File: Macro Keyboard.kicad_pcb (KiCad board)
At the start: 2 copper layers, 101.6 x 123.4 mm, 132 parts, among them J2901 FPC 1x24, Q2901 Q_PJFET_GDS, SW1001 KH-PS1611-54, SW1101 KH-PS1611-54, SW1201 KH-PS1611-54, SW1301 KH-PS1611-54, SW1401 KH-PS1611-54, SW1501 KH-PS1611-54, SW2801 SWITCH TACTILE SPST-NO 50MA 1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, SW601 KH-PS1611-54, SW701 KH-PS1611-54, SW801 KH-PS1611-54, SW901 KH-PS1611-54, U2701 PCA9745BTWJ, U2801 Pico-JER, U301 VEML7700, U401 PI4ULS5V201TAEX

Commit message: Moved everything to the back that I wanted. Added fun things :)
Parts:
- removed the Ref** at (116.8, 32.8)
- added Ref**: Val**, Macro Keyboard:TMPCB Logo bottom silk 10mm, F.Cu at (133.3, 42.8)
- added svg2mod: G***, Macro Keyboard:kilroy, F.Cu at (82.8, 137.0)
- added svg2mod: G***, Macro Keyboard:xkcd-swing, F.Cu at (97.8, 111.0)
- added svg2mod: G***, Macro Keyboard:xkcd-climb, F.Cu at (106.4, 44.4)
- added svg2mod: G***, Macro Keyboard:xkcd, F.Cu at (110.2, 72.9)
- C2701, C2801, C2901, C2902, C2903, C2907, C2908, C2909, C301, C401, C402, D2901, D2902, D2903, L2901, Q2901, R208, R209, R2704, R2705, R2706, R2707, R2801, R2902, R301, R302, U2701, U401: moved to B.Cu
- moved D2901 23.7 mm to (95.5, 50.8), turned to 22.5 degrees
- moved DS** 23.6 mm to (73.0, 59.5)
- moved D2903 23.1 mm to (94.9, 47.6)
- moved R2801 20.1 mm to (103.2, 26.3), turned to 45 degrees
- moved C2906 15.0 mm to (117.1, 74.3), turned to 90 degrees
- moved C2907 14.2 mm to (115.1, 74.3), turned to 270 degrees
- moved R2703 12.6 mm to (131.7, 69.1), turned to 0 degrees
- moved U301 12.5 mm to (92.8, 38.6), turned to 90 degrees
- moved C2701 11.8 mm to (130.8, 64.5)
- moved C2903 11.5 mm to (113.0, 74.3), turned to 270 degrees
- moved R2704 11.2 mm to (131.7, 71.1), turned to 0 degrees
- moved C2905 9.65 mm to (100.1, 52.0), turned to 0 degrees
- moved R302 7.30 mm to (97.7, 36.4), turned to 90 degrees
- moved R2706 7.22 mm to (128.4, 60.0)
- moved C401 7.05 mm to (136.9, 51.2), turned to 0 degrees
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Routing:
- net GND: track 117.9 -> 188.2 mm, vias 114 -> 120
- net /eInk Display/DS_VGH: track 7.88 -> 41.7 mm, vias 0 -> 2
- net Net-(C2902-Pad2): track 44.5 -> 12.8 mm, vias 2 -> 0
- net /eInk Display/DS_VGL: track 10.5 -> 41.9 mm, vias 0 -> 2
- net +5V: track 336.2 -> 359.3 mm, vias 7 -> 3
- net /eInk Display/DS_VDDD: track 5.58 -> 21.9 mm
- net /eInk Display/DS_MOSFET_S: track 31.9 -> 16.2 mm, vias 4 -> 0
- net /RGB Driver/DRIVER_LED_CS_3V3: track 48.4 -> 63.5 mm, vias 2 -> 0
- net /Pico/GPIO_14: track 64.7 -> 49.9 mm, vias 4 -> 2
- net /RGB Driver/DRIVER_LED_SW2_G_5V: track 54.5 -> 40.3 mm, vias 0 -> 1
- net /eInk Display/DS_VSH: track 6.16 -> 19.4 mm, vias 0 -> 1
- net /RGB Driver/DRIVER_LED_SW2_B_5V: track 53.6 -> 40.3 mm, vias 0 -> 1
- net /Pico/GPIO_20: track 60.7 -> 48.2 mm, vias 1 -> 2
- net /Level Converter/D_IN_3V3: track 87.6 -> 99.5 mm, vias 1 -> 2
- net SPI_MISO_3V: track 24.5 -> 36.3 mm, vias 1 -> 0
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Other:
- board text added: "0"
- board text added: "1"
- board text added: "2"
- board text added: "Designed in Washington State"
- board text added: "IF YOU CAN READ THIS, THERE IS A PROBLEM …OR MAYBE THE BOARD HAS NOT BEEN ASSEMBLED"
- board text added: "pew pew"
- board text added: "π"

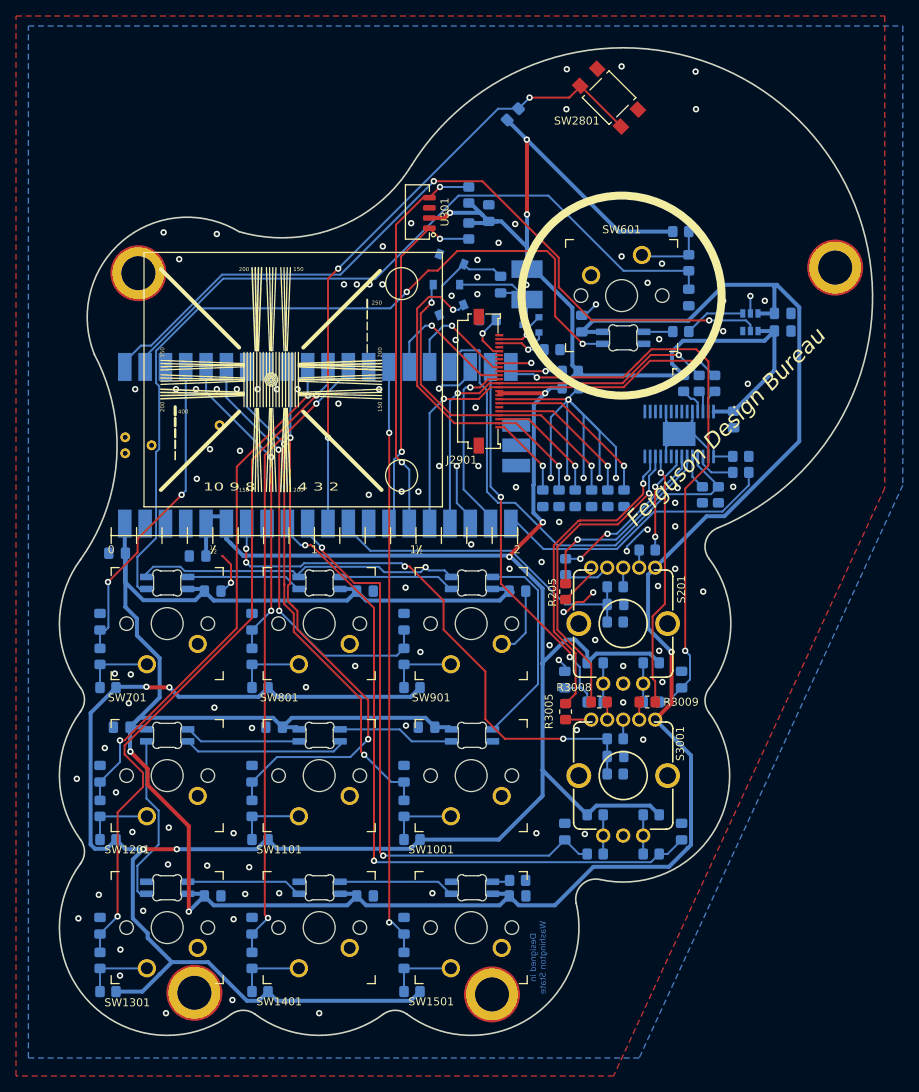
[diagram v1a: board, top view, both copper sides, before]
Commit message: Updated silkscreen outlines. Added epaper cad part.
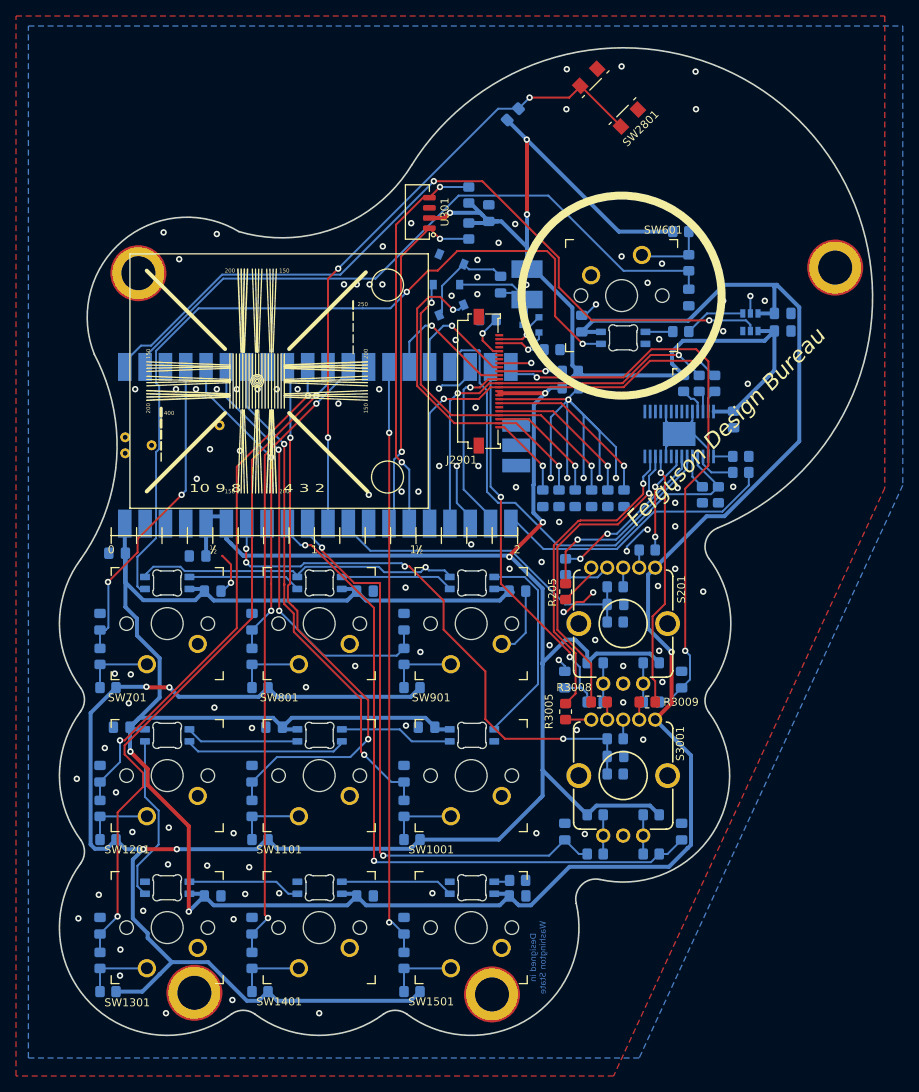
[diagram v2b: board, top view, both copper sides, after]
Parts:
- moved DS** 1.77 mm to (71.2, 59.7)
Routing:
- net +5V: track 359.3 -> 358.7 mm

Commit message: Add Solder Mask Clearance
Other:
- rule pad_to_mask_clearance: 0 -> 0.00129
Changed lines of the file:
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@@
   (layers
     (0 F.Cu signal)
-    (31 B.Cu signal hide)
+    (31 B.Cu signal)
     (32 B.Adhes user hide)
     (33 F.Adhes user hide)
@@
     (mod_text_size 1 1)
     (mod_text_width 0.15)
-    (pad_size 1.524 1.524)
-    (pad_drill 0.762)
-    (pad_to_mask_clearance 0)
+    (pad_size 1.7018 1.7018)
+    (pad_drill 1.7018)
+    (pad_to_mask_clearance 0.00129)
     (aux_axis_origin 0 0)
     (visible_elements FFFFFF7F)

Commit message: Add Solder Mask Clearance
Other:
- rule pad_to_mask_clearance: 0.00129 -> 0.0508
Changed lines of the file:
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@@
     (pad_size 1.7018 1.7018)
     (pad_drill 1.7018)
-    (pad_to_mask_clearance 0.00129)
+    (pad_to_mask_clearance 0.0508)
+    (solder_mask_min_width 0.1016)
     (aux_axis_origin 0 0)
     (visible_elements FFFFFF7F)

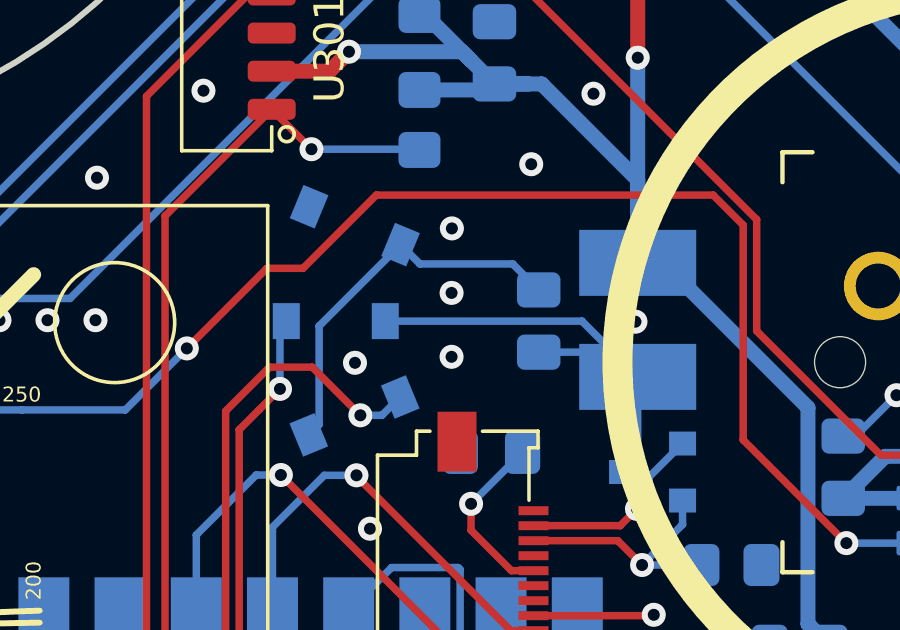
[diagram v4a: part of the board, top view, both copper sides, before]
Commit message: Move D2903 to allow for extra clearance
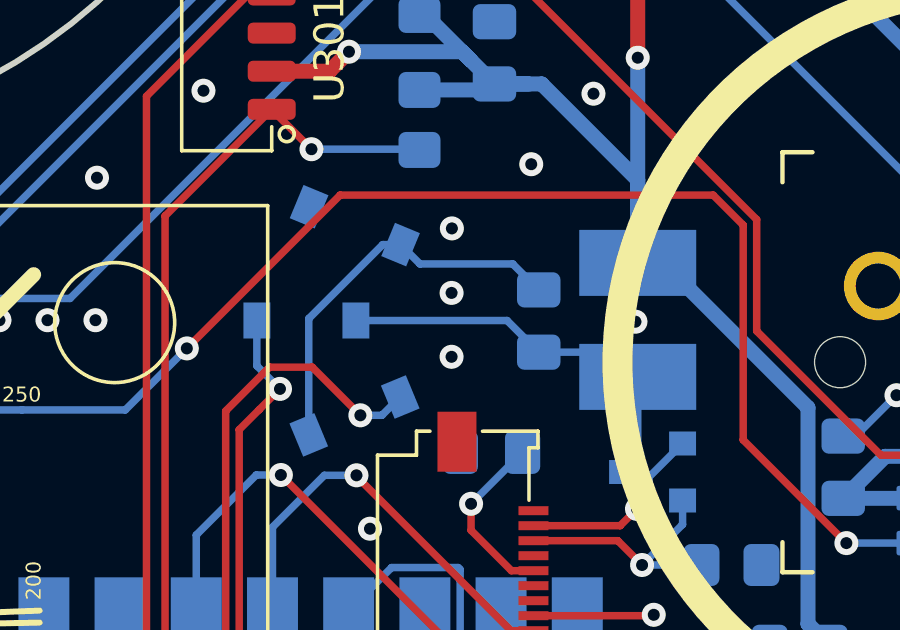
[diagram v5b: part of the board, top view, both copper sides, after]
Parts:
- moved D2903 0.98 mm to (93.9, 47.6)
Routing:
- net /eInk Display/DS_MOSFET_S: track 16.2 -> 13.6 mm
- net GND: vias 120 -> 119
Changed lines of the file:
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@@
     (thickness 1.6)
     (drawings 92)
-    (tracks 1019)
+    (tracks 1015)
     (zones 0)
     (modules 136)
@@
     (32 B.Adhes user hide)
     (33 F.Adhes user hide)
-    (34 B.Paste user hide)
-    (35 F.Paste user)
-    (36 B.SilkS user hide)
-    (37 F.SilkS user)
-    (38 B.Mask user hide)
-    (39 F.Mask user)
-    (40 Dwgs.User user)
+    (34 B.Paste user)
+    (35 F.Paste user hide)
+    (36 B.SilkS user)
+    (37 F.SilkS user hide)
+    (38 B.Mask user)
+    (39 F.Mask user hide)
+    (40 Dwgs.User user hide)
     (41 Cmts.User user hide)
     (42 Eco1.User user hide)
@@
     (44 Edge.Cuts user)
     (45 Margin user hide)
-    (46 B.CrtYd user hide)
-    (47 F.CrtYd user)
-    (48 B.Fab user hide)
-    (49 F.Fab user)
+    (46 B.CrtYd user)
+    (47 F.CrtYd user hide)
+    (48 B.Fab user)
+    (49 F.Fab user hide)
   )
   (setup
@@
   )
   (module Diode_SMD:D_SOD-123 placed (layer B.Cu)
-    (at 94.91 47.63)
+    (at 93.93 47.61)
     (descr SOD-123)
     (tags SOD-123)
@@
   (via (at 93.97 60.62) (size 0.8) (drill 0.4) (layers F.Cu B.Cu) (net 1))
   (via (at 98.78 44.54) (size 0.8) (drill 0.4) (layers F.Cu B.Cu) (net 1))
-  (via (at 95.55 49.02) (size 0.8) (drill 0.4) (layers F.Cu B.Cu) (net 1))
   (via (at 98.9 70.3) (size 0.8) (drill 0.4) (layers F.Cu B.Cu) (net 1))
   (via (at 96.2 70.3) (size 0.8) (drill 0.4) (layers F.Cu B.Cu) (net 1))
@@
   (segment (start 97.714999 45.724999) (end 97.07 45.08) (width 0.25) (layer B.Cu) (net 17) (status 20))
   (segment (start 101.675 46.59) (end 100.809999 45.724999) (width 0.25) (layer B.Cu) (net 17) (status 10))
-  (segment (start 94.354415 51.078441) (end 94.01 51.422856) (width 0.25) (layer B.Cu) (net 17) (status 30))
-  (segment (start 94.354415 47.795585) (end 94.354415 51.078441) (width 0.25) (layer B.Cu) (net 17) (status 20))
-  (segment (start 97.07 45.08) (end 94.354415 47.795585) (width 0.25) (layer B.Cu) (net 17) (status 10))
+  (segment (start 96.474998 45.08) (end 94.01 47.544998) (width 0.25) (layer B.Cu) (net 17))
+  (segment (start 94.01 47.544998) (end 94.01 51.422856) (width 0.25) (layer B.Cu) (net 17))
+  (segment (start 97.07 45.08) (end 96.474998 45.08) (width 0.25) (layer B.Cu) (net 17))
   (segment (start 111.930001 55.029999) (end 111.93 55.03) (width 0.25) (layer B.Cu) (net 18))
   (via (at 111.93 55.03) (size 0.8) (drill 0.4) (layers F.Cu B.Cu) (net 18))
   (segment (start 114.4 55.029999) (end 111.930001 55.029999) (width 0.25) (layer B.Cu) (net 18) (status 10))
-  (segment (start 111.93 55.03) (end 108.49 51.59) (width 0.25) (layer F.Cu) (net 18))
-  (segment (start 108.49 51.59) (end 108.49 44.43) (width 0.25) (layer F.Cu) (net 18))
-  (segment (start 108.49 44.43) (end 107.49 43.43) (width 0.25) (layer F.Cu) (net 18))
-  (segment (start 107.49 43.43) (end 96.26 43.43) (width 0.25) (layer F.Cu) (net 18))
-  (segment (start 96.26 43.43) (end 93.82 45.87) (width 0.25) (layer F.Cu) (net 18))
-  (segment (start 93.82 45.87) (end 92.62 45.87) (width 0.25) (layer F.Cu) (net 18))
   (segment (start 58.604999 68.561003) (end 59.000001 68.166001) (width 0.25) (layer B.Cu) (net 18))
   (segment (start 58.604999 59.930001) (end 58.604999 55.909999) (width 0.25) (layer B.Cu) (net 18))
@@
   (segment (start 63.924998 50.59) (end 58.604999 55.909999) (width 0.25) (layer B.Cu) (net 18))
   (via (at 89.945 48.54) (size 0.8) (drill 0.4) (layers F.Cu B.Cu) (net 18))
-  (segment (start 92.615 45.87) (end 89.945 48.54) (width 0.25) (layer F.Cu) (net 18))
   (segment (start 89.945 48.54) (end 87.895 50.59) (width 0.25) (layer B.Cu) (net 18))
   (segment (start 84.45 50.59) (end 63.924998 50.59) (width 0.25) (layer B.Cu) (net 18))
   (segment (start 87.895 50.59) (end 84.45 50.59) (width 0.25) (layer B.Cu) (net 18))
-  (segment (start 92.62 45.87) (end 92.615 45.87) (width 0.25) (layer F.Cu) (net 18))
+  (segment (start 95.055 43.43) (end 89.945 48.54) (width 0.25) (layer F.Cu) (net 18))
+  (segment (start 107.49 43.43) (end 95.055 43.43) (width 0.25) (layer F.Cu) (net 18))
+  (segment (start 108.49 44.43) (end 107.49 43.43) (width 0.25) (layer F.Cu) (net 18))
+  (segment (start 108.49 51.59) (end 108.49 44.43) (width 0.25) (layer F.Cu) (net 18))
+  (segment (start 111.93 55.03) (end 108.49 51.59) (width 0.25) (layer F.Cu) (net 18))
   (segment (start 123.170001 53.529999) (end 123.2 53.5) (width 0.25) (layer B.Cu) (net 19) (status 30))
   (segment (start 119.6 53.529999) (end 123.170001 53.529999) (width 0.25) (layer B.Cu) (net 19) (status 30))
@@
   (segment (start 113.05 70.275) (end 106.725 63.95) (width 0.25) (layer F.Cu) (net 102))
   (via (at 93.05 49.89) (size 0.8) (drill 0.4) (layers F.Cu B.Cu) (net 102))
-  (segment (start 93.05 47.84) (end 93.26 47.63) (width 0.25) (layer B.Cu) (net 102) (status 30))
-  (segment (start 93.05 49.89) (end 93.05 47.84) (width 0.25) (layer B.Cu) (net 102) (status 20))
   (segment (start 92.354999 50.585001) (end 93.05 49.89) (width 0.25) (layer F.Cu) (net 102))
   (segment (start 95.54 63.95) (end 91.69001 60.10001) (width 0.25) (layer F.Cu) (net 102))
@@
   (segment (start 101.5 63.95) (end 95.54 63.95) (width 0.25) (layer F.Cu) (net 102) (status 10))
   (segment (start 91.69001 51.24999) (end 92.354999 50.585001) (width 0.25) (layer F.Cu) (net 102))
+  (segment (start 92.28 49.12) (end 93.05 49.89) (width 0.25) (layer B.Cu) (net 102))
+  (segment (start 92.28 47.61) (end 92.28 49.12) (width 0.25) (layer B.Cu) (net 102))
   (via (at 99.42 53.72) (size 0.8) (drill 0.4) (layers F.Cu B.Cu) (net 103))
   (segment (start 101.1375 52.0025) (end 99.42 53.72) (width 0.25) (layer B.Cu) (net 103) (status 10))
@@
   (segment (start 105.349999 53.490001) (end 105.349999 52.830001) (width 0.25) (layer B.Cu) (net 109))
   (segment (start 104.95 53.89) (end 105.349999 53.490001) (width 0.25) (layer B.Cu) (net 109))
-  (segment (start 103.115 47.63) (end 104.975 49.49) (width 0.25) (layer B.Cu) (net 110) (status 20))
-  (segment (start 96.56 47.63) (end 103.115 47.63) (width 0.25) (layer B.Cu) (net 110) (status 10))
   (segment (start 104.15 48.665) (end 104.975 49.49) (width 0.25) (layer B.Cu) (net 110) (status 30))
   (segment (start 101.675 48.665) (end 104.15 48.665) (width 0.25) (layer B.Cu) (net 110) (status 30))
   (segment (start 104.975 52.155) (end 104.47 52.66) (width 0.25) (layer B.Cu) (net 110) (status 20))
   (segment (start 104.975 49.49) (end 104.975 52.155) (width 0.25) (layer B.Cu) (net 110) (status 10))
+  (segment (start 100.62 47.61) (end 95.58 47.61) (width 0.25) (layer B.Cu) (net 110))
+  (segment (start 101.675 48.665) (end 100.62 47.61) (width 0.25) (layer B.Cu) (net 110))
   (via (at 105.12 55.76) (size 0.8) (drill 0.4) (layers F.Cu B.Cu) (net 111))
   (segment (start 104.31 54.95) (end 105.12 55.76) (width 0.25) (layer F.Cu) (net 111))

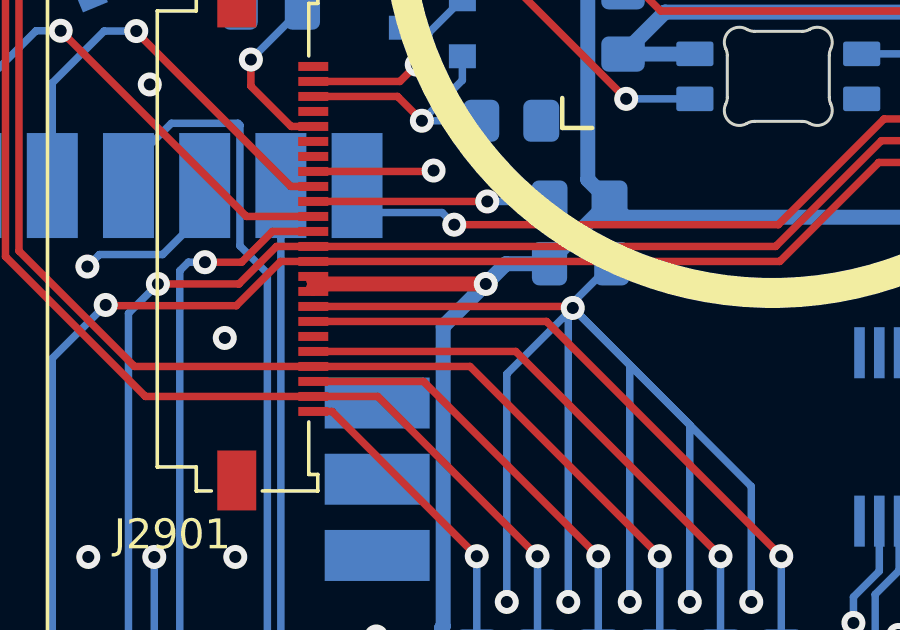
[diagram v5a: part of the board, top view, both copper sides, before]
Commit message: Update GND connection on J2901 to remove sliver
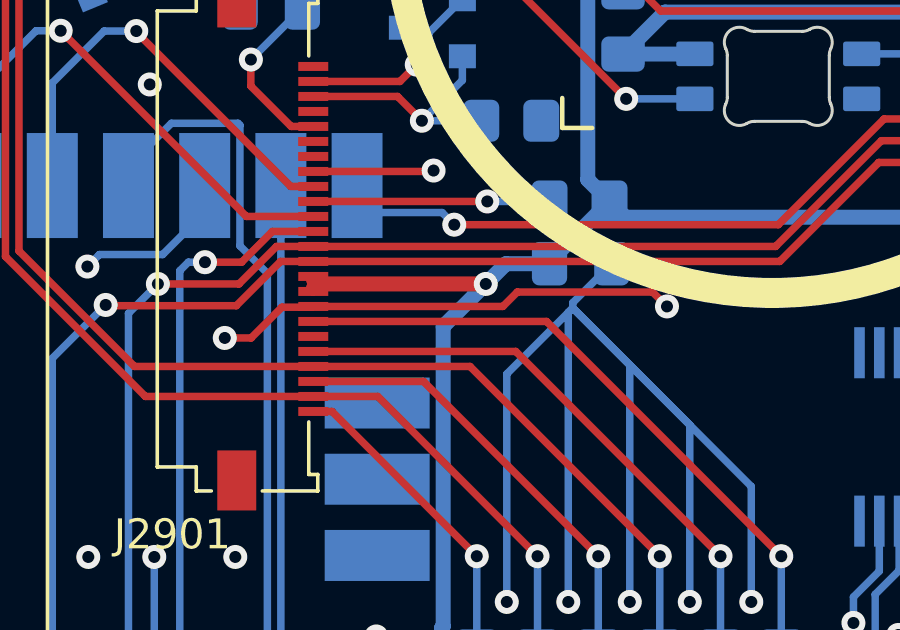
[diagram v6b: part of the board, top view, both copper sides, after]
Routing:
- net GND: track 188.2 -> 195.1 mm
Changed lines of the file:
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@@
     (thickness 1.6)
     (drawings 92)
-    (tracks 1015)
+    (tracks 1022)
     (zones 0)
     (modules 136)
@@
   (via (at 90.5 39.95) (size 0.8) (drill 0.4) (layers F.Cu B.Cu) (net 1))
   (via (at 103.5 40.05) (size 0.8) (drill 0.4) (layers F.Cu B.Cu) (net 1))
-  (segment (start 110.1 61.95) (end 110.15 62) (width 0.25) (layer F.Cu) (net 1))
-  (via (at 110.15 62) (size 0.8) (drill 0.4) (layers F.Cu B.Cu) (net 1))
-  (segment (start 101.5 61.95) (end 110.1 61.95) (width 0.25) (layer F.Cu) (net 1) (status 10))
   (segment (start 110.15 61.825) (end 111.45 60.525) (width 0.25) (layer B.Cu) (net 1) (status 20))
   (segment (start 110.15 62) (end 110.15 61.825) (width 0.25) (layer B.Cu) (net 1))
@@
   (via (at 85.3 47.6) (size 0.8) (drill 0.4) (layers F.Cu B.Cu) (net 1))
   (segment (start 109.1 55.47) (end 109.1 55.47) (width 0.25) (layer B.Cu) (net 1))
+  (segment (start 101.47 61.95) (end 101.445001 61.974999) (width 0.25) (layer F.Cu) (net 1))
+  (segment (start 101.445001 61.974999) (end 100.455001 61.974999) (width 0.25) (layer F.Cu) (net 1))
+  (segment (start 101.5 61.95) (end 101.47 61.95) (width 0.25) (layer F.Cu) (net 1))
+  (segment (start 99.43 63) (end 98.55 63) (width 0.25) (layer F.Cu) (net 1))
+  (segment (start 100.455001 61.974999) (end 99.43 63) (width 0.25) (layer F.Cu) (net 1))
+  (via (at 113.29 61.95) (size 0.8) (drill 0.4) (layers F.Cu B.Cu) (net 1))
+  (segment (start 101.5 61.95) (end 107.82 61.95) (width 0.25) (layer F.Cu) (net 1))
+  (segment (start 107.82 61.95) (end 108.3 61.47) (width 0.25) (layer F.Cu) (net 1))
+  (segment (start 112.81 61.47) (end 113.29 61.95) (width 0.25) (layer F.Cu) (net 1))
+  (segment (start 108.3 61.47) (end 112.81 61.47) (width 0.25) (layer F.Cu) (net 1))
   (segment (start 109.7 98.0375) (end 110.7375 98.0375) (width 0.25) (layer B.Cu) (net 2) (status 10))
   (segment (start 112.5 98.75) (end 111.775 98.025) (width 0.25) (layer B.Cu) (net 2))
